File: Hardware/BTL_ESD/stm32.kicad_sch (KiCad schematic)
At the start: 1 part, among them U3 STM32F103RCTx

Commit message: hardware: ver 1 schematic
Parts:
- added C17, C18, C20, C21: 20pF/50V, Capacitor_SMD:C_0603_1608Metric_Pad1.08x0.95mm_HandSolder, symbol Device:C_Small
- added C19: 10uF/16V, Capacitor_SMD:C_0603_1608Metric_Pad1.08x0.95mm_HandSolder, symbol Device:C_Small
- added C22, C23, C27, C28, C29, C31, C32, C34, C35, C36, C37: 100nF/16V, Capacitor_SMD:C_0603_1608Metric_Pad1.08x0.95mm_HandSolder, symbol Device:C_Small
- added C24, C33: 10nF/50V, Capacitor_SMD:C_0603_1608Metric_Pad1.08x0.95mm_HandSolder, symbol Device:C_Small
- added C25, C30: 1uF/16V, Capacitor_SMD:C_0603_1608Metric_Pad1.08x0.95mm_HandSolder, symbol Device:C_Small
- added C26: 4.7uF/25V, Capacitor_SMD:C_0603_1608Metric_Pad1.08x0.95mm_HandSolder, symbol Device:C_Small
- added D7: Green, LED_SMD:LED_0805_2012Metric_Pad1.15x1.40mm_HandSolder, symbol Device:LED
- added J2: Load Program, Connector_PinHeader_2.54mm:PinHeader_1x04_P2.54mm_Vertical, symbol Connector:Conn_01x04_Pin
- added R11, R12, R14: 10k/1%, Resistor_SMD:R_0603_1608Metric_Pad0.98x0.95mm_HandSolder, symbol Device:R_Small_US
- added R13: 10k/1%, Resistor_SMD:R_0603_1608Metric_Pad0.98x0.95mm_HandSolder, symbol Device:R_US
- added SW2: RESET, Button_Switch_SMD:SW_SPST_B3U-1000P, symbol Switch:SW_Push
- added Y1: 8MHz, Crystal:Crystal_SMD_EuroQuartz_MQ-4Pin_7.0x5.0mm, symbol Device:Crystal_GND24_Small
- added Y2: 32.768KHz, Crystal:Crystal_SMD_3215-2Pin_3.2x1.5mm, symbol Device:Crystal_Small
- renumbered U3 to U4
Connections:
- net +3V3: now reaches U4.1 (VBAT)
- net +3V3: now also U4.13 (VDDA), U4.19 (VDD), U4.32 (VDD), U4.48 (VDD), U4.64 (VDD), C19.1, C23.1, C26.1, C27.1, C28.1, C29.1, C30.1, C31.1, C32.1, C33.1, C34.1, C35.1, C36.1, C37.1, J2.1 (Pin_1), R11.1
- net GND: now reaches U4.12 (VSSA)
- net GND: now also U4.18 (VSS), U4.31 (VSS), U4.47 (VSS), U4.63 (VSS), C17.2, C18.2, C19.2, C20.2, C21.2, C22.1, C23.2, C24.2, C25.2, C26.2, C27.2, C28.2, C29.2, C30.2, C31.2, C32.2, C33.2, C34.2, C35.2, C36.2, C37.2, J2.4 (Pin_4), R12.2, R14.2, SW2.1, Y1.2, Y1.4
- net ADC1_0: now reaches U4.14 (PA0)
- net ADC1_0: now also C24.1, C25.1
- net TFT_IRQ: now reaches U4.15 (PA1)
- net TFT_DC_RS: now reaches U4.16 (PA2)
- net TFT_RESET: now reaches U4.17 (PA3)
- net LED_TEST: now reaches U4.2 (PC13)
- net LED_TEST: now also D7.2 (A)
- net SPI1_CS: now reaches U4.20 (PA4)
- net SPI1_SCLK: now reaches U4.21 (PA5)
- net SPI1_MISO: now reaches U4.22 (PA6)
- net SPI1_MOSI: now reaches U4.23 (PA7)
- net OSC32_IN: now reaches U4.3 (PC14)
- net OSC32_IN: now also C18.1, Y2.1
- net SPI2_CS: now reaches U4.33 (PB12)
- net SPI2_SCLK: now reaches U4.34 (PB13)
- net SPI2_MISO: now reaches U4.35 (PB14)
- net SPI2_MOSI: now reaches U4.36 (PB15)
- net OSC32_OUT: now reaches U4.4 (PC15)
- net OSC32_OUT: now also C20.1, Y2.2
- net TFT_BL: now reaches U4.41 (PA8)
- net CONTROL_LED: now reaches U4.42 (PA9)
- net SWDIO: now reaches U4.46 (PA13)
- net SWDIO: now also J2.2 (Pin_2)
- net SWCLK: now reaches U4.49 (PA14)
- net SWCLK: now also J2.3 (Pin_3)
- net OSC_IN: now reaches U4.5 (PD0)
- net OSC_IN: now also C17.1, Y1.1
- net RXD: now reaches U4.51 (PC10)
- net TXD: now reaches U4.52 (PC11)
- net OSC_OUT: now reaches U4.6 (PD1)
- net OSC_OUT: now also C21.1, Y1.3
- net BOOT: now reaches U4.60 (BOOT0)
- net BOOT: now also R11.2, R12.1
- net RESET: now reaches U4.7 (NRST)
- net RESET: now also C22.2, R13.2, SW2.2
- new net: D7.1 (K), R14.1
- new net +3.3V: R13.1
- no-connect marks 0 -> 28
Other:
- note added: "LOAD PROGRAM"
- note added: "OSC"
- note added: "RESET - BOOT"
- title: (none) -> STM32
- moved on the sheet: U4

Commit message: update
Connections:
- net GND: no longer C17.2, C18.2, C20.2, C21.2, Y1.2, Y1.4
- new net GND1: C17.2, C18.2, C20.2, C21.2, Y1.2, Y1.4
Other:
- moved on the sheet: C26, C27, C28, C29, C30, C31, C32, C33, C34, C35, C36, C37

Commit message: update
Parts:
- added D8: BZT52C3V3-7-F, BZT52C3V3-7-F:BZT52C3V3, symbol BZT52C3V3-7-F:BZT52C3V3-7-F
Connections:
- net ADC1_0: now also D8.K
- net GND: now also D8.A
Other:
- moved on the sheet: C24, C25

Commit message: fea:STM32: upload structure fodler
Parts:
- added J2: BOOT, Connector_PinHeader_2.54mm:PinHeader_1x03_P2.54mm_Vertical, symbol Connector:Conn_01x03_Pin
- added R15: Uart_Conn, UART:uart_conn, symbol uart:uart_conn
- renumbered J2 to J3
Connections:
- net BOOT: now also J2.2 (Pin_2); no longer R11.2, R12.1
- net CONTROL_LED: now also U4.41 (PA8); no longer U4.42 (PA9)
- net TFT_BL: now also U4.42 (PA9); no longer U4.41 (PA8)
- net GPIO_1: now reaches U4.24 (PC4)
- net GPIO_2: now reaches U4.25 (PC5)
- net RXD renamed UART4_TX
- net UART4_TX: now also R15.1 (TX_OUT)
- net TXD renamed UART4_RX
- net UART4_RX: now also R15.4 (RX_OUT)
- new net: J2.1 (Pin_1), R11.2
- new net: J2.3 (Pin_3), R12.1
- new net RXD_2: R15.2 (RX_IN)
- new net TXD_2: R15.3 (TX_IN)
- no-connect marks 28 -> 26
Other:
- moved on the sheet: R11, R12

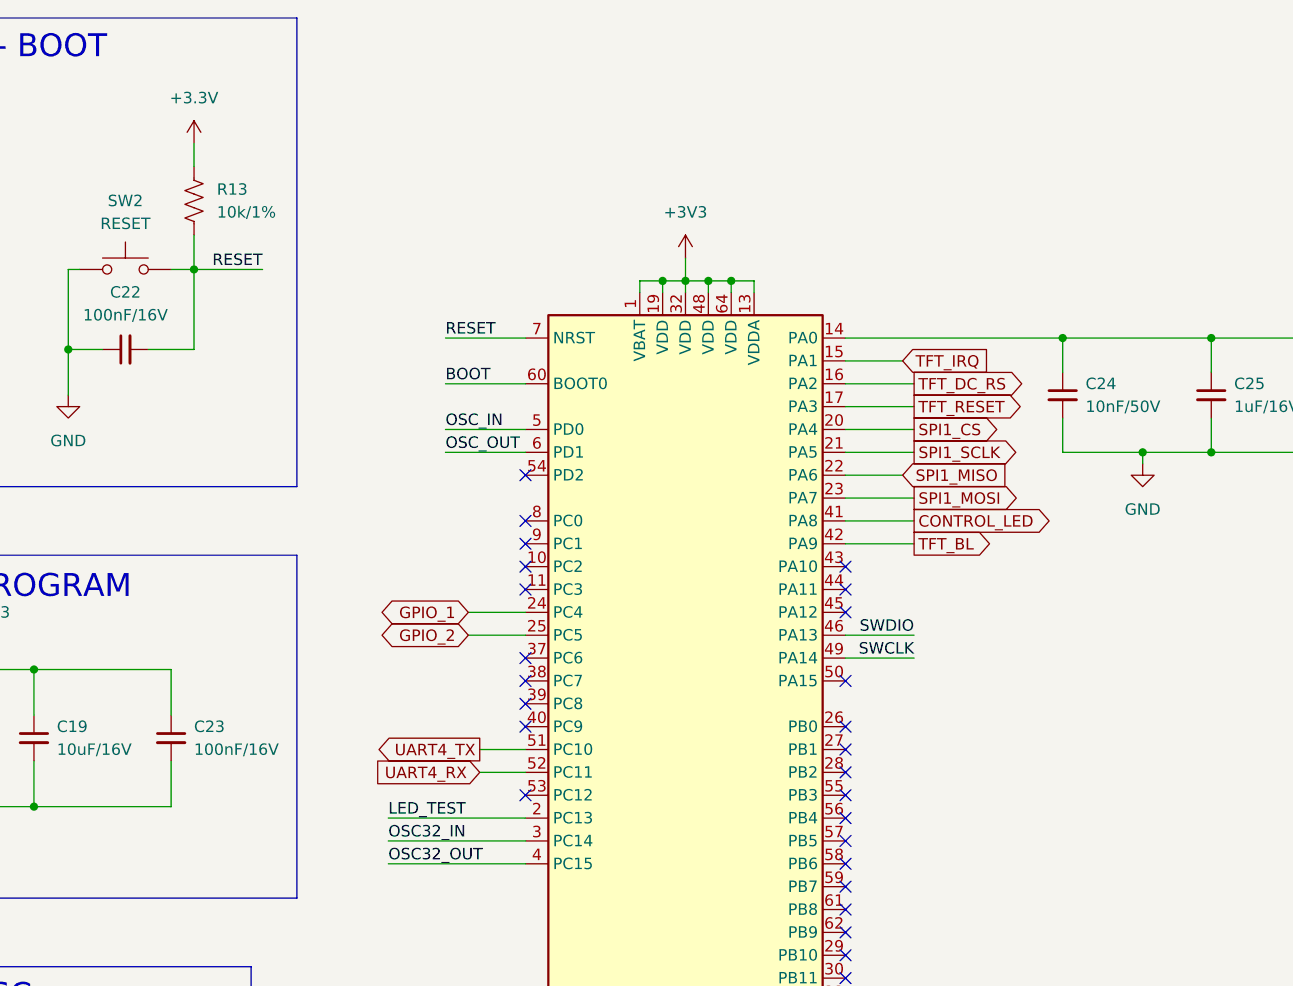
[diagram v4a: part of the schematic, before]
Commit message: hardware:update pcb track power
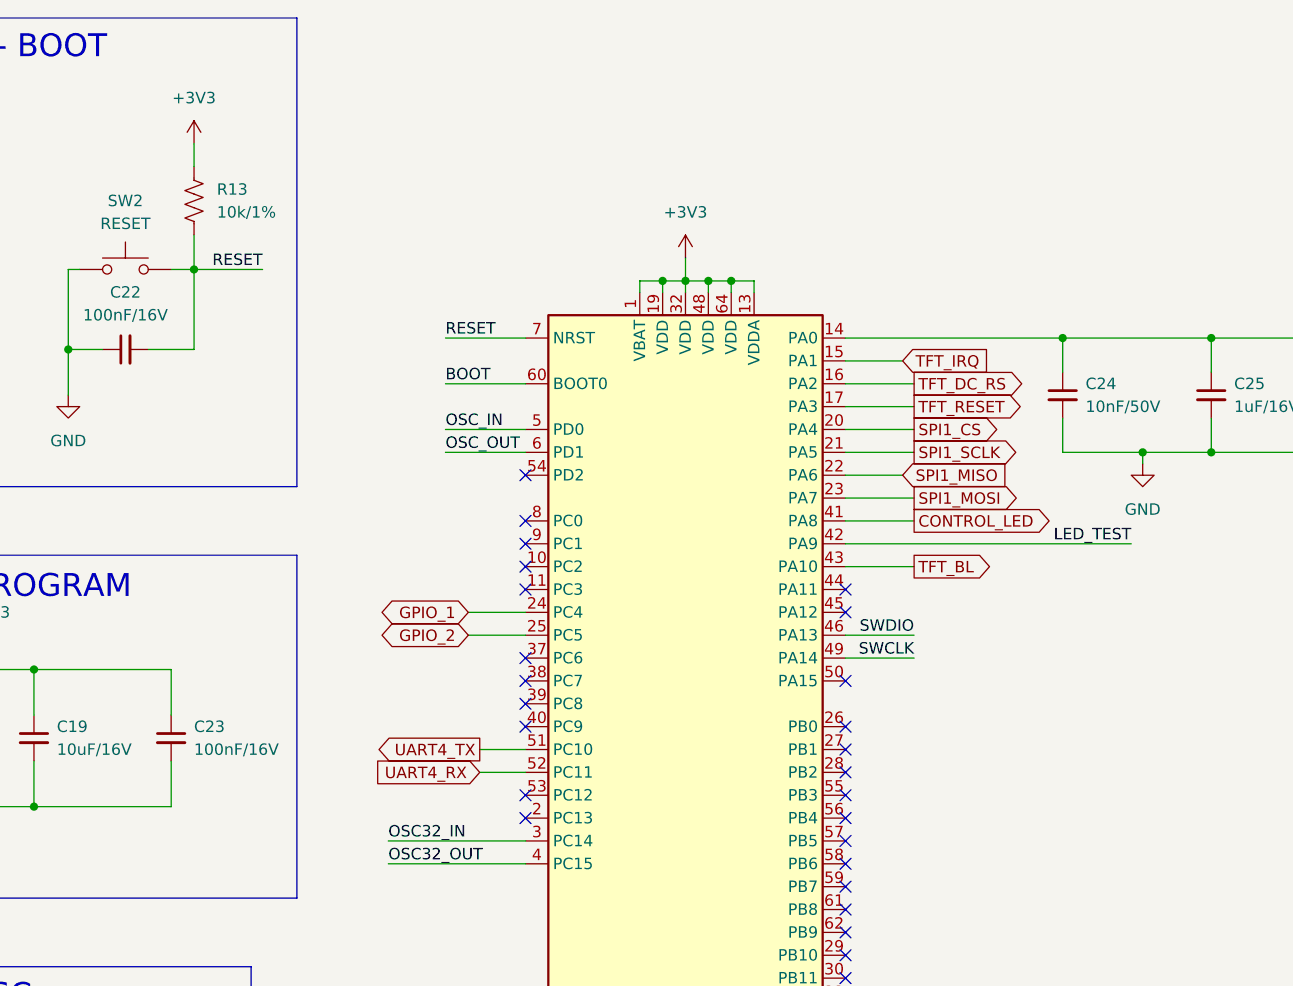
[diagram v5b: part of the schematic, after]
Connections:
- net +3.3V is gone; now on net +3V3: R13.1
- net LED_TEST: now also U4.42 (PA9); no longer U4.2 (PC13)
- net TFT_BL: now also U4.43 (PA10); no longer U4.42 (PA9)

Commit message: code:ESP32: update uart driver, main.c && hardware file pcb
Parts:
- added R15, R16: 0/1%, Resistor_SMD:R_0603_1608Metric_Pad0.98x0.95mm_HandSolder, symbol Device:R_US
- added R17: 10k/1%, Resistor_SMD:R_0603_1608Metric_Pad0.98x0.95mm_HandSolder, symbol Device:R_Small_US
- renumbered R15 to R18
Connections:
- net CONTROL_LED: now also U4.37 (PC6); no longer U4.41 (PA8)
- net GND: now also R17.2
- net LED_TEST: now also U4.38 (PC7); no longer U4.42 (PA9)
- net TFT_BL: now also U4.39 (PC8); no longer U4.43 (PA10)
- net UART4_RX: now also R15.2
- net UART4_TX: now also R16.2
- net at U4.28 (PB2): now also R17.1
- net BOOT renamed BOOT0
- new net: R16.1, U4.42 (PA9)
- new net: R15.1, U4.43 (PA10)
- no-connect marks 26 -> 23
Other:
- moved on the sheet: D8
